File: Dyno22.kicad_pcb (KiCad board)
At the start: 2 copper layers, 53 parts, among them J1 Pwr Input, J2 Display, J3 Pwr Output, J4 BPM & Sensors, J7 UART, SW1 SW_DPST_x2, U1 TS2937CW50, U2 LM324, U3 Demux

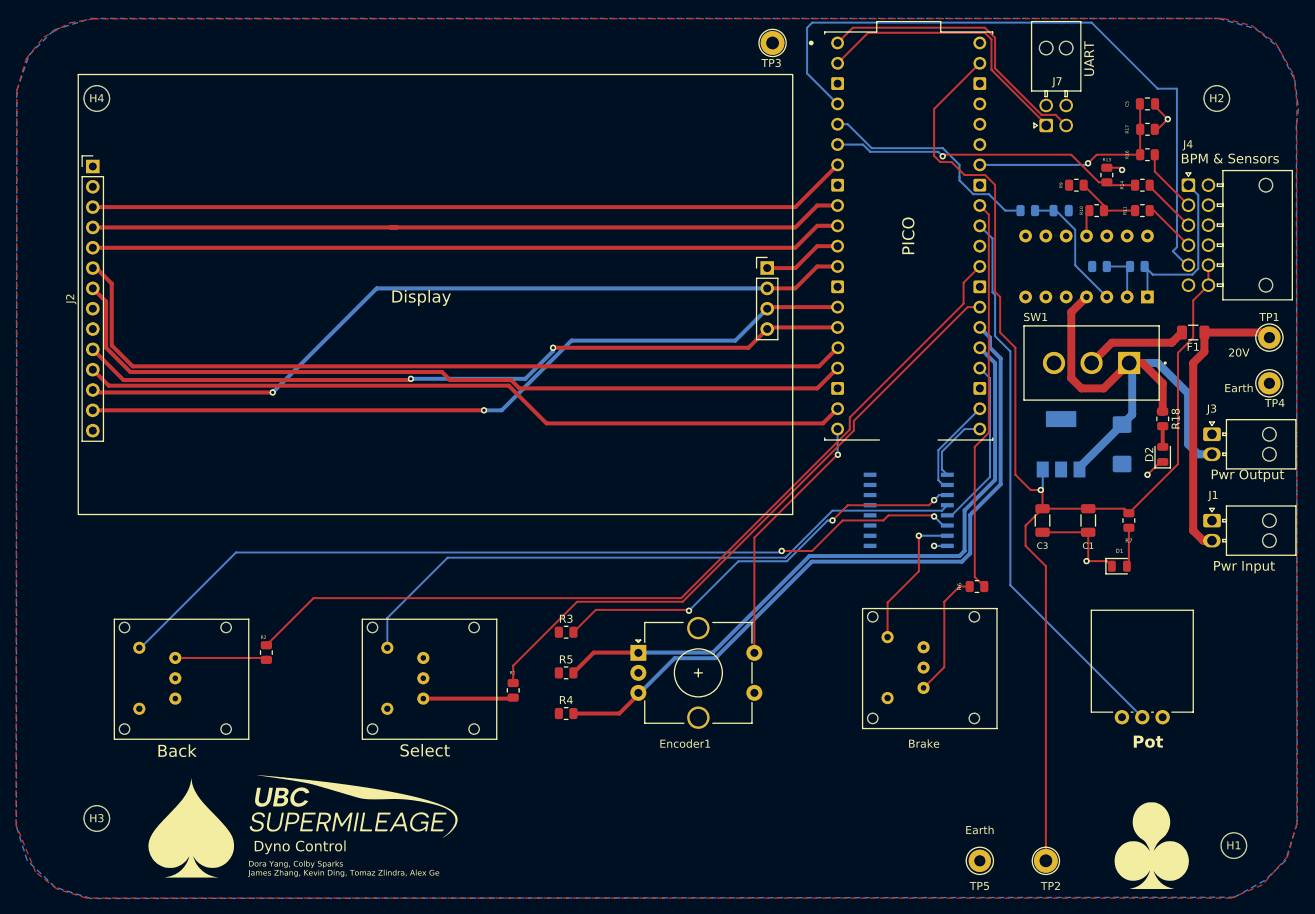
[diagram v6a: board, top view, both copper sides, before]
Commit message: PCB trace routing changes
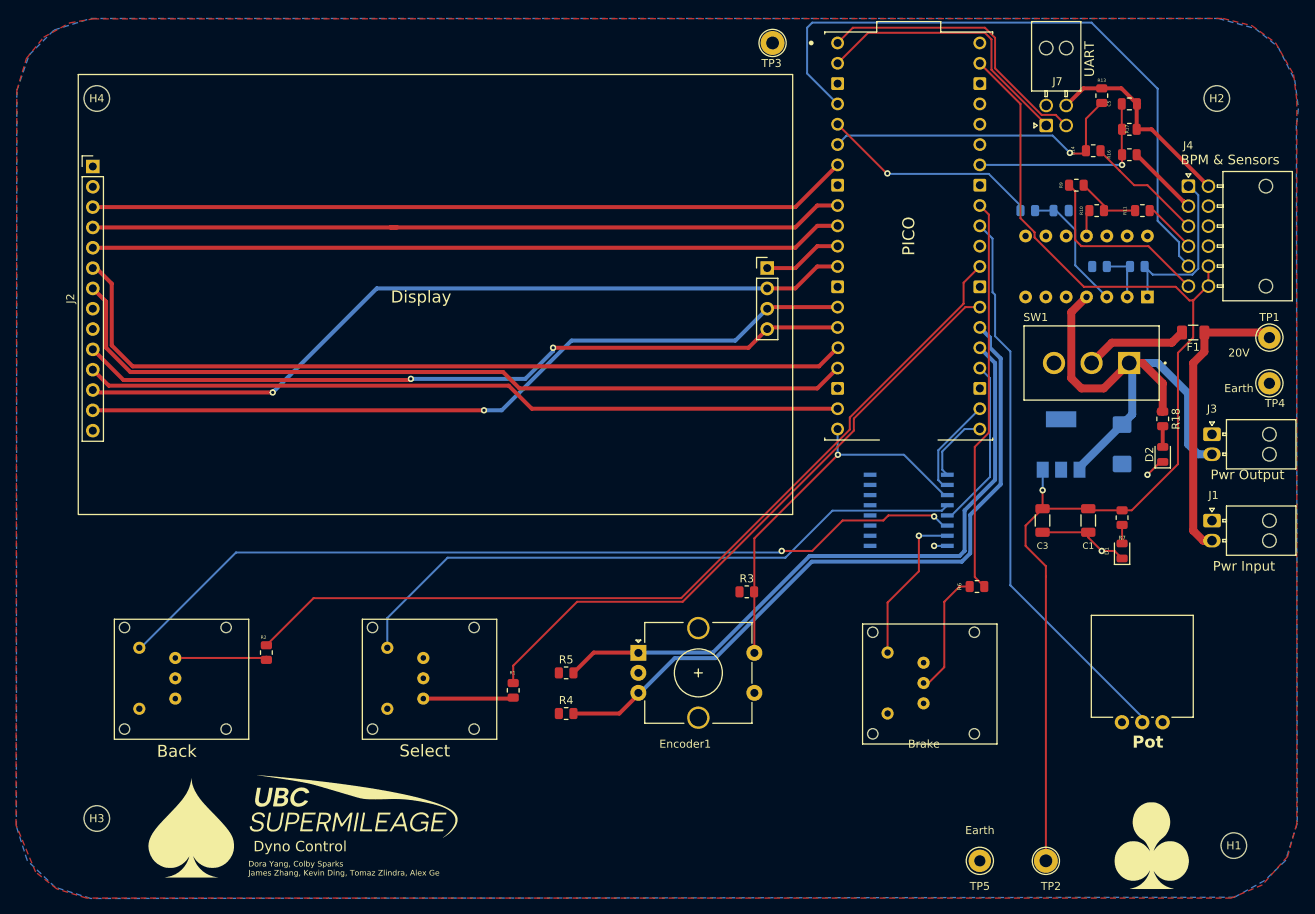
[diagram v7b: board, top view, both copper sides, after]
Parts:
- moved R3 23.1 mm to (153.7, 104.2)
- moved R13 9.95 mm to (198.1, 42.1)
- moved R14 7.50 mm to (197.1, 49.0)
- moved C5 2.26 mm to (201.6, 43.2)
- moved R16 2.26 mm to (201.6, 49.5)
- moved R17 2.26 mm to (201.6, 46.4)
- moved D1 1.93 mm to (200.7, 99.1), turned to 90 degrees
- moved S3 1.93 mm to (168.2, 108.2)
- moved R7 0.92 mm to (200.7, 94.9)
- moved RV1 0.63 mm to (205.7, 120.5)
- moved J4 0.12 mm to (209.0, 53.5)
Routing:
- net /ROT_EN_SW: track 86.3 -> 49.3 mm, vias 4 -> 1
- net +3.3V: track 1.65 -> 25.4 mm
- net Earth: track 26.3 -> 44.1 mm, vias 4 -> 2
- net +5V: track 161.5 -> 144.6 mm
- net /OP_SIG: track 7.01 -> 15.0 mm
- net Net-(D1-A): track 4.85 -> 2.32 mm
- net /KILL_SW: track 84.8 -> 82.9 mm
- net /BTN_BRAKE: track 17.9 -> 19.8 mm
- net /TOUCH_CS: track 96.6 -> 95.1 mm
- net /FORCE_IN: track 26.9 -> 25.4 mm
- net /FORCE_SIG: track 8.05 -> 9.13 mm
- net /BPM_CTRL_OUT: track 28.9 -> 28.4 mm, vias 0 -> 1

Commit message: Trace changes
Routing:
- net +5V: track 144.6 -> 151.7 mm, vias 1 -> 3
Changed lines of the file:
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@@
   (segment (start 144.74 112.46) (end 140.44 116.76) (width 0.5) (layer "B.Cu") (net 24))
   (segment (start 181.675 99.34995) (end 180.62995 100.395) (width 0.5) (layer "B.Cu") (net 24))
+  (segment (start 185.4562 54.767123) (end 185.42 54.803323) (width 0.25) (layer "F.Cu") (net 27))
   (segment (start 188.595 98.425) (end 191.135 100.965) (width 0.25) (layer "F.Cu") (net 27))
-  (segment (start 187.96 43.182792) (end 187.96 57.464009) (width 0.25) (layer "F.Cu") (net 27))
+  (segment (start 208.96496 67.739366) (end 209.083933 67.745) (width 0.25) (layer "F.Cu") (net 27))
+  (segment (start 209.083933 67.745) (end 209.55 67.745) (width 0.25) (layer "F.Cu") (net 27))
   (segment (start 182.88 38.1) (end 182.88 38.102792) (width 0.25) (layer "F.Cu") (net 27))
-  (segment (start 189.72 59.224009) (end 189.72 59.865991) (width 0.25) (layer "F.Cu") (net 27))
   (segment (start 190.71619 93.775) (end 196.43119 93.775) (width 0.25) (layer "F.Cu") (net 27))
   (segment (start 191.135 102.235) (end 191.135 137.795) (width 0.25) (layer "F.Cu") (net 27))
-  (segment (start 195.894009 66.04) (end 207.373299 66.04) (width 0.25) (layer "F.Cu") (net 27))
-  (segment (start 187.96 57.464009) (end 189.72 59.224009) (width 0.25) (layer "F.Cu") (net 27))
+  (segment (start 209.072665 67.745) (end 208.96496 67.739366) (width 0.25) (layer "F.Cu") (net 27))
+  (segment (start 185.42 54.803323) (end 185.42 54.924009) (width 0.25) (layer "F.Cu") (net 27))
   (segment (start 200.66 93.98) (end 201.86869 93.98) (width 0.25) (layer "F.Cu") (net 27))
   (segment (start 190.727627 91.467528) (end 190.71619 93.775) (width 0.25) (layer "F.Cu") (net 27))
+  (segment (start 182.88 38.102792) (end 185.42 40.642792) (width 0.25) (layer "F.Cu") (net 27))
   (segment (start 211.455 65.84) (end 211.455 63.34) (width 0.25) (layer "F.Cu") (net 27))
   (segment (start 200.66 93.98) (end 196.63619 93.98) (width 0.25) (layer "F.Cu") (net 27))
   (segment (start 209.55 67.745) (end 211.455 65.84) (width 0.25) (layer "F.Cu") (net 27))
+  (segment (start 209.078299 67.745) (end 209.072665 67.745) (width 0.25) (layer "F.Cu") (net 27))
   (segment (start 207.645 88.20369) (end 207.645 74.295) (width 0.25) (layer "F.Cu") (net 27))
-  (segment (start 189.72 59.865991) (end 195.894009 66.04) (width 0.25) (layer "F.Cu") (net 27))
   (segment (start 191.135 100.965) (end 191.135 102.235) (width 0.25) (layer "F.Cu") (net 27))
   (segment (start 201.86869 93.98) (end 207.645 88.20369) (width 0.25) (layer "F.Cu") (net 27))
+  (segment (start 185.42 40.642792) (end 185.42 54.730923) (width 0.25) (layer "F.Cu") (net 27))
   (segment (start 209.55 72.39) (end 209.55 67.745) (width 0.25) (layer "F.Cu") (net 27))
-  (segment (start 207.373299 66.04) (end 209.078299 67.745) (width 0.25) (layer "F.Cu") (net 27))
-  (segment (start 182.88 38.102792) (end 187.96 43.182792) (width 0.25) (layer "F.Cu") (net 27))
+  (segment (start 185.42 54.730923) (end 185.4562 54.767123) (width 0.25) (layer "F.Cu") (net 27))
   (segment (start 190.71619 91.65619) (end 190.727627 91.467528) (width 0.25) (layer "F.Cu") (net 27))
   (segment (start 196.63619 93.98) (end 196.43119 93.775) (width 0.25) (layer "F.Cu") (net 27))
   (segment (start 190.71619 93.775) (end 188.595 95.89619) (width 0.25) (layer "F.Cu") (net 27))
-  (segment (start 209.078299 67.745) (end 209.55 67.745) (width 0.25) (layer "F.Cu") (net 27))
   (segment (start 207.645 74.295) (end 209.55 72.39) (width 0.25) (layer "F.Cu") (net 27))
   (segment (start 188.595 95.89619) (end 188.595 98.425) (width 0.25) (layer "F.Cu") (net 27))
+  (via (at 185.4562 54.767123) (size 0.8) (drill 0.4) (layers "F.Cu" "B.Cu") (net 27))
   (via (at 190.727627 91.467528) (size 0.8) (drill 0.4) (layers "F.Cu" "B.Cu") (net 27))
+  (via (at 208.96496 67.739366) (size 0.8) (drill 0.4) (layers "F.Cu" "B.Cu") (net 27))
+  (segment (start 208.96496 67.739366) (end 208.124326 68.58) (width 0.25) (layer "B.Cu") (net 27))
+  (segment (start 208.124326 68.58) (end 187.96 68.58) (width 0.25) (layer "B.Cu") (net 27))
+  (segment (start 187.96 68.58) (end 185.42 66.04) (width 0.25) (layer "B.Cu") (net 27))
+  (segment (start 185.42 54.803323) (end 185.4562 54.767123) (width 0.25) (layer "B.Cu") (net 27))
   (segment (start 190.74 88.9) (end 190.74 91.455155) (width 0.25) (layer "B.Cu") (net 27))
+  (segment (start 185.42 66.04) (end 185.42 54.803323) (width 0.25) (layer "B.Cu") (net 27))
   (segment (start 190.74 91.455155) (end 190.727627 91.467528) (width 0.25) (layer "B.Cu") (net 27))
   (segment (start 196.215 67.31) (end 194.31 69.215) (width 1) (layer "F.Cu") (net 29))
